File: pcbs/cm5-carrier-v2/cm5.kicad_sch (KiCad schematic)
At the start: 24 parts, among them J702 JST-SH-4-Vertical, Q701 DMN21D2UFB-7B, SW701 TS20-42-25-WT-160-SMT-TR, U702 NX3DV221GM

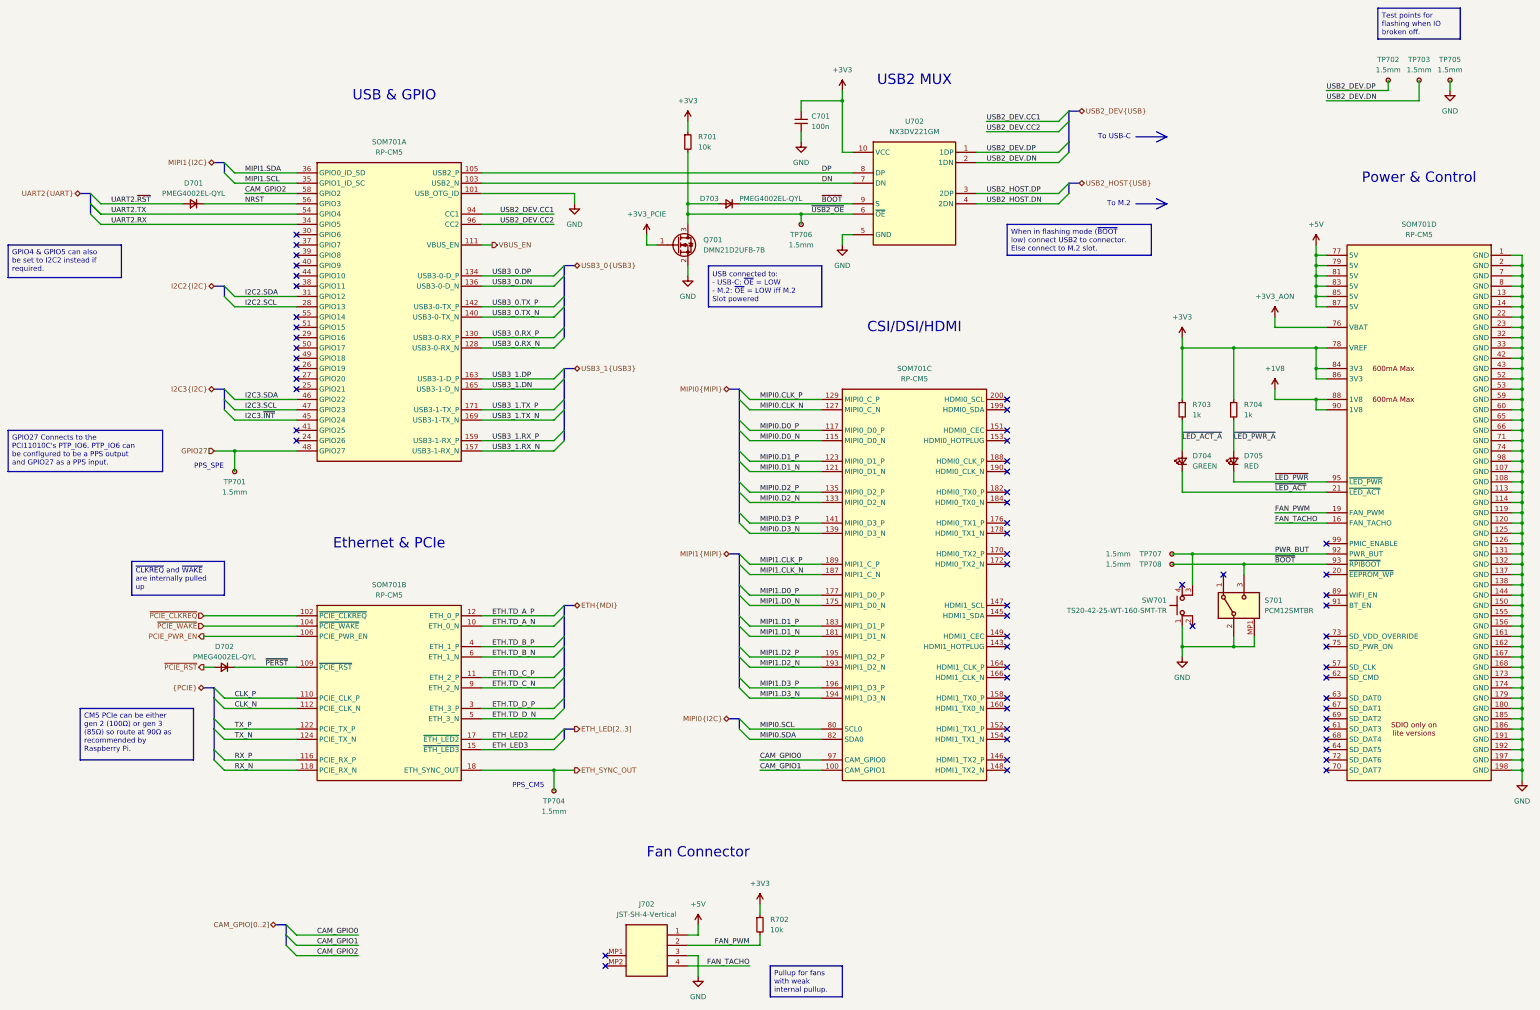
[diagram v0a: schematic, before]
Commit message: Changed UART connector to I2C
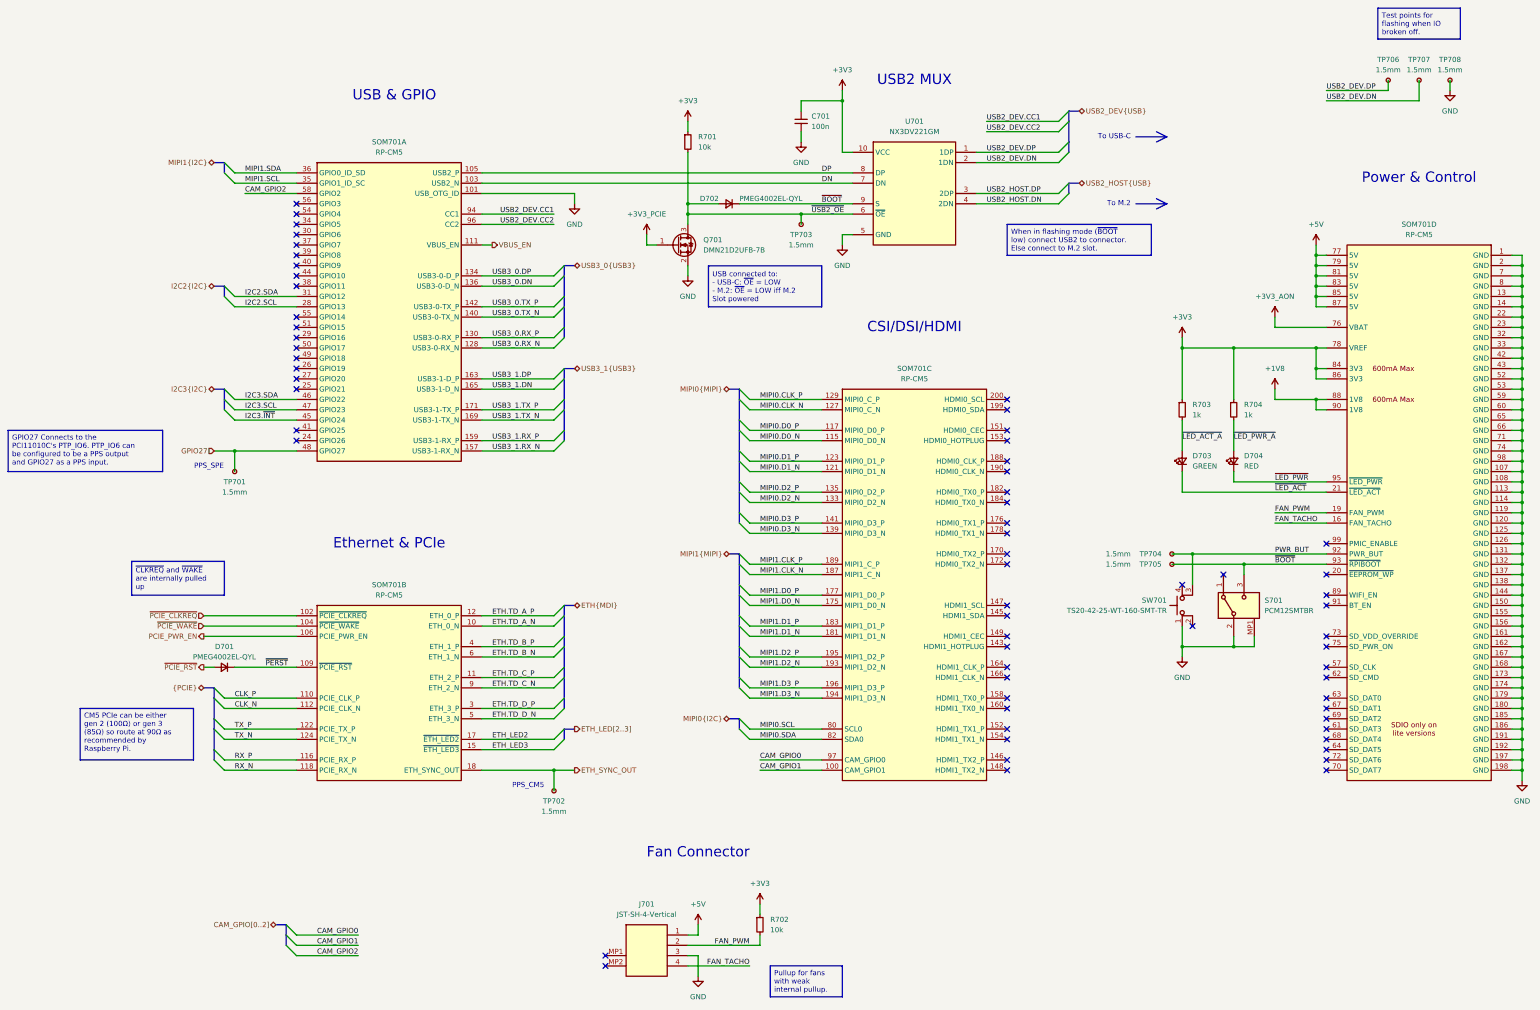
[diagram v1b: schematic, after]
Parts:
- removed D701: PMEG4002EL-QYL, project_footprints:PMEG4002EL-QYL, symbol DIODE:PMEG4002EL-QYL
- renumbered D702 to D701, D703 to D702, D704 to D703, D705 to D704, J702 to J701, TP704 to TP702, TP706 to TP703, TP707 to TP704, TP708 to TP705, TP702 to TP706, TP703 to TP707, TP705 to TP708, U702 to U701
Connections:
- net NRST: no longer names the net of SOM701.56 (GPIO3)
- net UART2.RX: no longer names the net of SOM701.34 (GPIO5)
- net UART2.TX: no longer names the net of SOM701.54 (GPIO4)
- no-connect marks 61 -> 64
